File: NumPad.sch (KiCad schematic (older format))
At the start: 63 parts, among them J1 Micro_SD_Card_Det, SW1 SW_SPST, SW10 SW_SPST, SW11 SW_SPST, SW12 SW_SPST, SW13 SW_SPST, SW14 SW_SPST, SW15 SW_SPST, SW16 SW_SPST, SW17 SW_SPST, SW18 SW_SPST, SW19 SW_SPST, SW2 SW_SPST, SW20 SW_SPST, SW21 SW_SPST, SW22 SW_SPST, SW23 SW_SPST, SW24 SW_SPST, SW3 SW_SPST, SW4 SW_SPST, SW5 SW_SPST, SW6 SW_SPST, SW7 SW_SPST, SW8 SW_SPST, SW9 SW_SPST, U1 LM117_TO3, U2 STM32F072C8Tx

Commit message: Update
Update before removing matrice
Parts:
- removed U?: UG-2864HSWEG01, symbol modules:UG-2864HSWEG01
- added J2: OLED1, symbol Connector:Conn_01x04_Female
- added J3: OLED2, symbol Connector:Conn_01x04_Female
- added J4: Conn_01x05_Female, symbol Connector:Conn_01x05_Female
- added R3, R4, R5, R6: 10K, symbol Device:R_Small
- added SW25: SW_BUTTONRESET, symbol Switch:SW_Push
- added SW26: SW_BUTTON2, symbol Switch:SW_Push
- added SW27: SW_BUTTON1, symbol Switch:SW_Push
- added SW28: SW_BOOT0, symbol Switch:SW_Push
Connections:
- net +3V3: now also J4.5 (Pin_5), R3.1, R4.1, R5.1, SW28.2
- net +5V: now also J2.4 (Pin_4), J3.4 (Pin_4)
- net GND: now also J2.3 (Pin_3), J3.3 (Pin_3), J4.4 (Pin_4), R6.2, SW25.1, SW26.2, SW27.2
- net col0: now also U2.40 (PB4)
- net col1: now also U2.41 (PB5)
- net col2: now also U2.42 (PB6)
- net col3: now also U2.43 (PB7)
- net row0: now also U2.26 (PB13)
- net row1: now also U2.27 (PB14)
- net row2: now also U2.28 (PB15)
- net row3: now also U2.29 (PA8)
- net row4: now also U2.38 (PA15)
- net row5: now also U2.39 (PB3)
- net at U2.11 (PA1): now also R4.2, SW27.1
- net at U2.13 (PA3): now also R5.2, SW26.1
- net UART1_TX: now reaches U2.30 (PA9)
- net UART1_TX: now also J4.3 (Pin_3)
- net LED_DATA_EN: now reaches U2.31 (PA10)
- net USB_DM: now reaches U2.32 (PA11)
- net USB_DP: now reaches U2.33 (PA12)
- net SYS_SWDIO: now reaches U2.34 (PA13)
- net SYS_SWDIO: now also J4.2 (Pin_2)
- net SYS_SWCLK: now reaches U2.37 (PA14)
- net SYS_SWCLK: now also J4.1 (Pin_1)
- net BOOT0: now reaches U2.44 (BOOT0)
- net SCK: now reaches U2.45 (PB8)
- net SCK: now also J2.2 (Pin_2), J3.2 (Pin_2)
- net SDA: now reaches U2.46 (PB9)
- net SDA: now also J2.1 (Pin_1), J3.1 (Pin_1)
- net at U2.7 (NRST): now also R3.2, SW25.2
- new net: R6.1, SW28.1

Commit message: Update
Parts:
- added C10, C11, C12, C13, C14, C7, C8, C9: 100nF, symbol Device:C_Small
- added D26, D27, D28, D29, D30, D31, D32, D33, D34, D35, D36, D37, D38, D39, D40, D41, D42, D43, D44, D45, D46, D47, D48, D49: SK6812MINIE, LED_SMD:LED_SK6812MINI_PLCC4_3.5x3.5mm_P1.75mm, symbol random-keyboard-parts:SK6812MINIE
- added R7, R8, R9: 10K, symbol Device:R_Small
- added RV1: 10K, symbol Device:R_POT
- added SW29: Rotary_Encoder, symbol Device:Rotary_Encoder
- added U3: 74AHCT1G08, symbol 74xGxx:74AHCT1G08
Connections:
- net D+ is gone; now on net USB_DP: D1.2 (I/O1), USB1.6 (DP1), USB1.8 (DP2)
- net GND is gone; now on net +5V: C3.2, C4.2, C5.2, C6.2, D1.1 (GND), J1.11 (SHIELD), J1.6 (VSS), J2.3 (Pin_3), J3.3 (Pin_3), J4.4 (Pin_4), R1.1, R2.1, R6.2, SW25.1, SW26.2, SW27.2, U2.1 (VBAT), U2.23 (VSS), U2.35 (VSS), U2.47 (VSS), U2.8 (VSSA), USB1.1 (GND), USB1.12 (GND), USB1.13 (SHIELD)
- net USB_DM is gone; now on net USB_DN: U2.32 (PA11)
- net +3V3: now also C10.1, C11.1, C12.1, C13.1, C14.1, C7.1, C8.1, C9.1, R8.2, R9.1, RV1.3
- net +5V: now also C1.2, C2.2, U1.1 (ADJ), C10.2, C11.2, C12.2, C13.2, C14.2, C7.2, C8.2, C9.2, D26.1 (VDD), D26.3 (VSS), D27.1 (VDD), D27.3 (VSS), D28.1 (VDD), D28.3 (VSS), D29.1 (VDD), D29.3 (VSS), D30.1 (VDD), D30.3 (VSS), D31.1 (VDD), D31.3 (VSS), D32.1 (VDD), D32.3 (VSS), D33.1 (VDD), D33.3 (VSS), D34.1 (VDD), D34.3 (VSS), D35.1 (VDD), D35.3 (VSS), D36.1 (VDD), D36.3 (VSS), D37.1 (VDD), D37.3 (VSS), D38.1 (VDD), D38.3 (VSS), D39.1 (VDD), D39.3 (VSS), D40.1 (VDD), D40.3 (VSS), D41.1 (VDD), D41.3 (VSS), D42.1 (VDD), D42.3 (VSS), D43.1 (VDD), D43.3 (VSS), D44.1 (VDD), D44.3 (VSS), D45.1 (VDD), D45.3 (VSS), D46.1 (VDD), D46.3 (VSS), D47.1 (VDD), D47.3 (VSS), D48.1 (VDD), D48.3 (VSS), D49.1 (VDD), D49.3 (VSS), R7.1, RV1.1, SW29.C, U3.3 (GND)
- net BOOT0: now also R6.1, SW28.1
- net LED_DATA_EN: now also R7.2, U3.1
- net SCK: now also U2.42 (PB6); no longer U2.45 (PB8)
- net SDA: now also U2.43 (PB7); no longer U2.46 (PB9)
- net SPI_MOSI: now also U3.2
- net VCC: now also U3.5 (VCC)
- net col0: now also U2.21 (PB10); no longer U2.40 (PB4)
- net col2: now also U2.22 (PB11); no longer U2.42 (PB6)
- net col3: now also U2.25 (PB12); no longer U2.43 (PB7)
- net row4: now also U2.12 (PA2); no longer U2.38 (PA15)
- net row5: now also U2.2 (PC13); no longer U2.39 (PB3)
- net D- renamed USB_DN
- new net: D26.2 (DOUT), D32.4 (DIN)
- new net: D26.4 (DIN), U3.4
- new net: D32.2 (DOUT), D38.4 (DIN)
- new net: D38.2 (DOUT), D44.4 (DIN)
- new net: D27.4 (DIN), D44.2 (DOUT)
- new net: D27.2 (DOUT), D33.4 (DIN)
- new net: D33.2 (DOUT), D39.4 (DIN)
- new net: D39.2 (DOUT), D45.4 (DIN)
- new net: D28.4 (DIN), D45.2 (DOUT)
- new net: D28.2 (DOUT), D34.4 (DIN)
- new net: D34.2 (DOUT), D40.4 (DIN)
- new net: D40.2 (DOUT), D46.4 (DIN)
- new net: D29.4 (DIN), D46.2 (DOUT)
- new net: D29.2 (DOUT), D35.4 (DIN)
- new net: D35.2 (DOUT), D41.4 (DIN)
- new net: D41.2 (DOUT), D47.4 (DIN)
- new net: D30.4 (DIN), D47.2 (DOUT)
- new net: D30.2 (DOUT), D36.4 (DIN)
- new net: D36.2 (DOUT), D42.4 (DIN)
- new net: D42.2 (DOUT), D48.4 (DIN)
- new net: D31.4 (DIN), D48.2 (DOUT)
- new net: D31.2 (DOUT), D37.4 (DIN)
- new net: D37.2 (DOUT), D43.4 (DIN)
- new net: D43.2 (DOUT), D49.4 (DIN)
- new net POT_SLIDER: RV1.2, U2.40 (PB4)
- new net TIM2_CH1: R8.1, SW29.A, U2.38 (PA15)
- new net TIM2_CH2: R9.2, SW29.B, U2.39 (PB3)
- no-connect marks 5 -> 16
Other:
- moved on the sheet: D10, D11, D12, D13, D14, D15, D16, D17, D18, D19, D2, D20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

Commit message: Update
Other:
- moved on the sheet: R4, R5, R6, SW26, SW27, SW28
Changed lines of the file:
@@
 L Switch:SW_Push SW27
 U 1 1 5E93AC97
-P 3300 5325
-F 0 "SW27" H 3300 5610 50  0000 C CNN
-F 1 "SW_BUTTON1" H 3300 5519 50  0000 C CNN
-F 2 "" H 3300 5525 50  0001 C CNN
-F 3 "~" H 3300 5525 50  0001 C CNN
-	1    3300 5325
+P 3575 5325
+F 0 "SW27" H 3575 5610 50  0000 C CNN
+F 1 "SW_BUTTON1" H 3575 5519 50  0000 C CNN
+F 2 "" H 3575 5525 50  0001 C CNN
+F 3 "~" H 3575 5525 50  0001 C CNN
+	1    3575 5325
 	1    0    0    -1
 $EndComp
@@
 L power:GND #PWR031
 U 1 1 5E940B20
-P 3575 5325
-F 0 "#PWR031" H 3575 5075 50  0001 C CNN
-F 1 "GND" H 3580 5152 50  0000 C CNN
-F 2 "" H 3575 5325 50  0001 C CNN
-F 3 "" H 3575 5325 50  0001 C CNN
-	1    3575 5325
-	1    0    0    -1
-$EndComp
-Wire Wire Line
-	3575 5325 3500 5325
+P 3850 5325
+F 0 "#PWR031" H 3850 5075 50  0001 C CNN
+F 1 "GND" H 3855 5152 50  0000 C CNN
+F 2 "" H 3850 5325 50  0001 C CNN
+F 3 "" H 3850 5325 50  0001 C CNN
+	1    3850 5325
+	1    0    0    -1
+$EndComp
+Wire Wire Line
+	3850 5325 3775 5325
 $Comp
 L power:+3.3V #PWR026
 U 1 1 5E945D9C
-P 2975 4850
-F 0 "#PWR026" H 2975 4700 50  0001 C CNN
-F 1 "+3.3V" H 2990 5023 50  0000 C CNN
-F 2 "" H 2975 4850 50  0001 C CNN
-F 3 "" H 2975 4850 50  0001 C CNN
-	1    2975 4850
+P 3250 4825
+F 0 "#PWR026" H 3250 4675 50  0001 C CNN
+F 1 "+3.3V" H 3265 4998 50  0000 C CNN
+F 2 "" H 3250 4825 50  0001 C CNN
+F 3 "" H 3250 4825 50  0001 C CNN
+	1    3250 4825
 	1    0    0    -1
 $EndComp
@@
 L Device:R_Small R4
 U 1 1 5E946CD8
-P 2975 5000
-F 0 "R4" H 3034 5046 50  0000 L CNN
-F 1 "10K" H 3034 4955 50  0000 L CNN
-F 2 "" H 2975 5000 50  0001 C CNN
-F 3 "~" H 2975 5000 50  0001 C CNN
-	1    2975 5000
-	1    0    0    -1
-$EndComp
-Wire Wire Line
-	2975 4850 2975 4900
+P 3250 4975
+F 0 "R4" H 3309 5021 50  0000 L CNN
+F 1 "10K" H 3309 4930 50  0000 L CNN
+F 2 "" H 3250 4975 50  0001 C CNN
+F 3 "~" H 3250 4975 50  0001 C CNN
+	1    3250 4975
+	1    0    0    -1
+$EndComp
+Wire Wire Line
+	3250 4825 3250 4875
 $Comp
 L Switch:SW_Push SW26
 U 1 1 5E9524FE
-P 3275 5925
-F 0 "SW26" H 3275 6210 50  0000 C CNN
-F 1 "SW_BUTTON2" H 3275 6119 50  0000 C CNN
-F 2 "" H 3275 6125 50  0001 C CNN
-F 3 "~" H 3275 6125 50  0001 C CNN
-	1    3275 5925
+P 3550 6125
+F 0 "SW26" H 3550 6410 50  0000 C CNN
+F 1 "SW_BUTTON2" H 3550 6319 50  0000 C CNN
+F 2 "" H 3550 6325 50  0001 C CNN
+F 3 "~" H 3550 6325 50  0001 C CNN
+	1    3550 6125
 	1    0    0    -1
 $EndComp
@@
 L power:GND #PWR032
 U 1 1 5E953574
-P 3575 5925
-F 0 "#PWR032" H 3575 5675 50  0001 C CNN
-F 1 "GND" H 3580 5752 50  0000 C CNN
-F 2 "" H 3575 5925 50  0001 C CNN
-F 3 "" H 3575 5925 50  0001 C CNN
-	1    3575 5925
-	1    0    0    -1
-$EndComp
-Wire Wire Line
-	3575 5925 3475 5925
+P 3850 6125
+F 0 "#PWR032" H 3850 5875 50  0001 C CNN
+F 1 "GND" H 3855 5952 50  0000 C CNN
+F 2 "" H 3850 6125 50  0001 C CNN
+F 3 "" H 3850 6125 50  0001 C CNN
+	1    3850 6125
+	1    0    0    -1
+$EndComp
+Wire Wire Line
+	3850 6125 3750 6125
 $Comp
 L power:+3.3V #PWR027
 U 1 1 5E95E2CA
-P 2975 5600
-F 0 "#PWR027" H 2975 5450 50  0001 C CNN
-F 1 "+3.3V" H 2990 5773 50  0000 C CNN
-F 2 "" H 2975 5600 50  0001 C CNN
-F 3 "" H 2975 5600 50  0001 C CNN
-	1    2975 5600
+P 3250 5825
+F 0 "#PWR027" H 3250 5675 50  0001 C CNN
+F 1 "+3.3V" H 3265 5998 50  0000 C CNN
+F 2 "" H 3250 5825 50  0001 C CNN
+F 3 "" H 3250 5825 50  0001 C CNN
+	1    3250 5825
 	1    0    0    -1
 $EndComp
@@
 L Device:R_Small R5
 U 1 1 5E95E6BD
-P 2975 5700
-F 0 "R5" H 2825 5800 50  0000 L CNN
-F 1 "10K" H 2775 5700 50  0000 L CNN
-F 2 "" H 2975 5700 50  0001 C CNN
-F 3 "~" H 2975 5700 50  0001 C CNN
-	1    2975 5700
-	1    0    0    -1
-$EndComp
-Wire Wire Line
-	3075 5925 2975 5925
-Wire Wire Line
-	2975 5925 2975 5800
+P 3250 5925
+F 0 "R5" H 3100 6025 50  0000 L CNN
+F 1 "10K" H 3050 5925 50  0000 L CNN
+F 2 "" H 3250 5925 50  0001 C CNN
+F 3 "~" H 3250 5925 50  0001 C CNN
+	1    3250 5925
+	1    0    0    -1
+$EndComp
 Wire Wire Line
 	2475 5800 2975 5800
-Connection ~ 2975 5800
-Wire Wire Line
-	3100 5325 2975 5325
-Wire Wire Line
-	2975 5100 2975 5325
-Connection ~ 2975 5325
-Wire Wire Line
-	2975 5325 2775 5325
 $Comp
 L power:GND #PWR024
@@
 L Switch:SW_Push SW28
 U 1 1 5E9A10FB
-P 3550 6625
-F 0 "SW28" H 3550 6910 50  0000 C CNN
-F 1 "SW_BOOT0" H 3550 6819 50  0000 C CNN
-F 2 "" H 3550 6825 50  0001 C CNN
-F 3 "~" H 3550 6825 50  0001 C CNN
-	1    3550 6625
+P 3700 7175
+F 0 "SW28" H 3700 7460 50  0000 C CNN
+F 1 "SW_BOOT0" H 3700 7369 50  0000 C CNN
+F 2 "" H 3700 7375 50  0001 C CNN
+F 3 "~" H 3700 7375 50  0001 C CNN
+	1    3700 7175
 	1    0    0    -1
 $EndComp
@@
 L power:+3.3V #PWR033
 U 1 1 5E9A1D5F
-P 3875 6625
-F 0 "#PWR033" H 3875 6475 50  0001 C CNN
-F 1 "+3.3V" H 3890 6798 50  0000 C CNN
-F 2 "" H 3875 6625 50  0001 C CNN
-F 3 "" H 3875 6625 50  0001 C CNN
-	1    3875 6625
-	1    0    0    -1
-$EndComp
-Wire Wire Line
-	3875 6625 3750 6625
+P 4025 7175
+F 0 "#PWR033" H 4025 7025 50  0001 C CNN
+F 1 "+3.3V" H 4040 7348 50  0000 C CNN
+F 2 "" H 4025 7175 50  0001 C CNN
+F 3 "" H 4025 7175 50  0001 C CNN
+	1    4025 7175
+	1    0    0    -1
+$EndComp
+Wire Wire Line
+	4025 7175 3900 7175
 $Comp
 L Device:R_Small R6
 U 1 1 5E9A85E3
-P 3300 6725
-F 0 "R6" H 3150 6825 50  0000 L CNN
-F 1 "10K" H 3100 6725 50  0000 L CNN
-F 2 "" H 3300 6725 50  0001 C CNN
-F 3 "~" H 3300 6725 50  0001 C CNN
-	1    3300 6725
-	1    0    0    -1
-$EndComp
-Wire Wire Line
-	3300 6625 3350 6625
+P 3450 7275
+F 0 "R6" H 3300 7375 50  0000 L CNN
+F 1 "10K" H 3250 7275 50  0000 L CNN
+F 2 "" H 3450 7275 50  0001 C CNN
+F 3 "~" H 3450 7275 50  0001 C CNN
+	1    3450 7275
+	1    0    0    -1
+$EndComp
+Wire Wire Line
+	3450 7175 3500 7175
 $Comp
 L power:GND #PWR028
 U 1 1 5E9AF02C
-P 3300 6900
-F 0 "#PWR028" H 3300 6650 50  0001 C CNN
-F 1 "GND" H 3305 6727 50  0000 C CNN
-F 2 "" H 3300 6900 50  0001 C CNN
-F 3 "" H 3300 6900 50  0001 C CNN
-	1    3300 6900
-	1    0    0    -1
-$EndComp
-Wire Wire Line
-	3300 6825 3300 6900
+P 3450 7450
+F 0 "#PWR028" H 3450 7200 50  0001 C CNN
+F 1 "GND" H 3455 7277 50  0000 C CNN
+F 2 "" H 3450 7450 50  0001 C CNN
+F 3 "" H 3450 7450 50  0001 C CNN
+	1    3450 7450
+	1    0    0    -1
+$EndComp
+Wire Wire Line
+	3450 7375 3450 7450
 $Comp
 L power:GND #PWR034
@@
 Text GLabel 1175 6100 0    50   Input ~ 0
 SCK
-Text GLabel 3300 6450 1    50   Input ~ 0
+Text GLabel 3450 7000 1    50   Input ~ 0
 BOOT0
 Wire Wire Line
-	3300 6450 3300 6625
-Connection ~ 3300 6625
+	3450 7000 3450 7175
+Connection ~ 3450 7175
 $Comp
 L random-keyboard-parts:SK6812MINIE D26
@@
 NoConn ~ 1175 6300
 NoConn ~ 1175 6400
-NoConn ~ 3775 5050
+NoConn ~ 12950 150
+Wire Wire Line
+	2975 6125 3250 6125
+Wire Wire Line
+	2975 5800 2975 6125
+Wire Wire Line
+	3250 6125 3250 6025
+Connection ~ 3250 6125
+Wire Wire Line
+	3250 6125 3350 6125
+Wire Wire Line
+	3250 5325 3250 5075
+Connection ~ 3250 5325
+Wire Wire Line
+	3250 5325 3375 5325
+Wire Wire Line
+	2775 5325 3250 5325
 $EndSCHEMATC

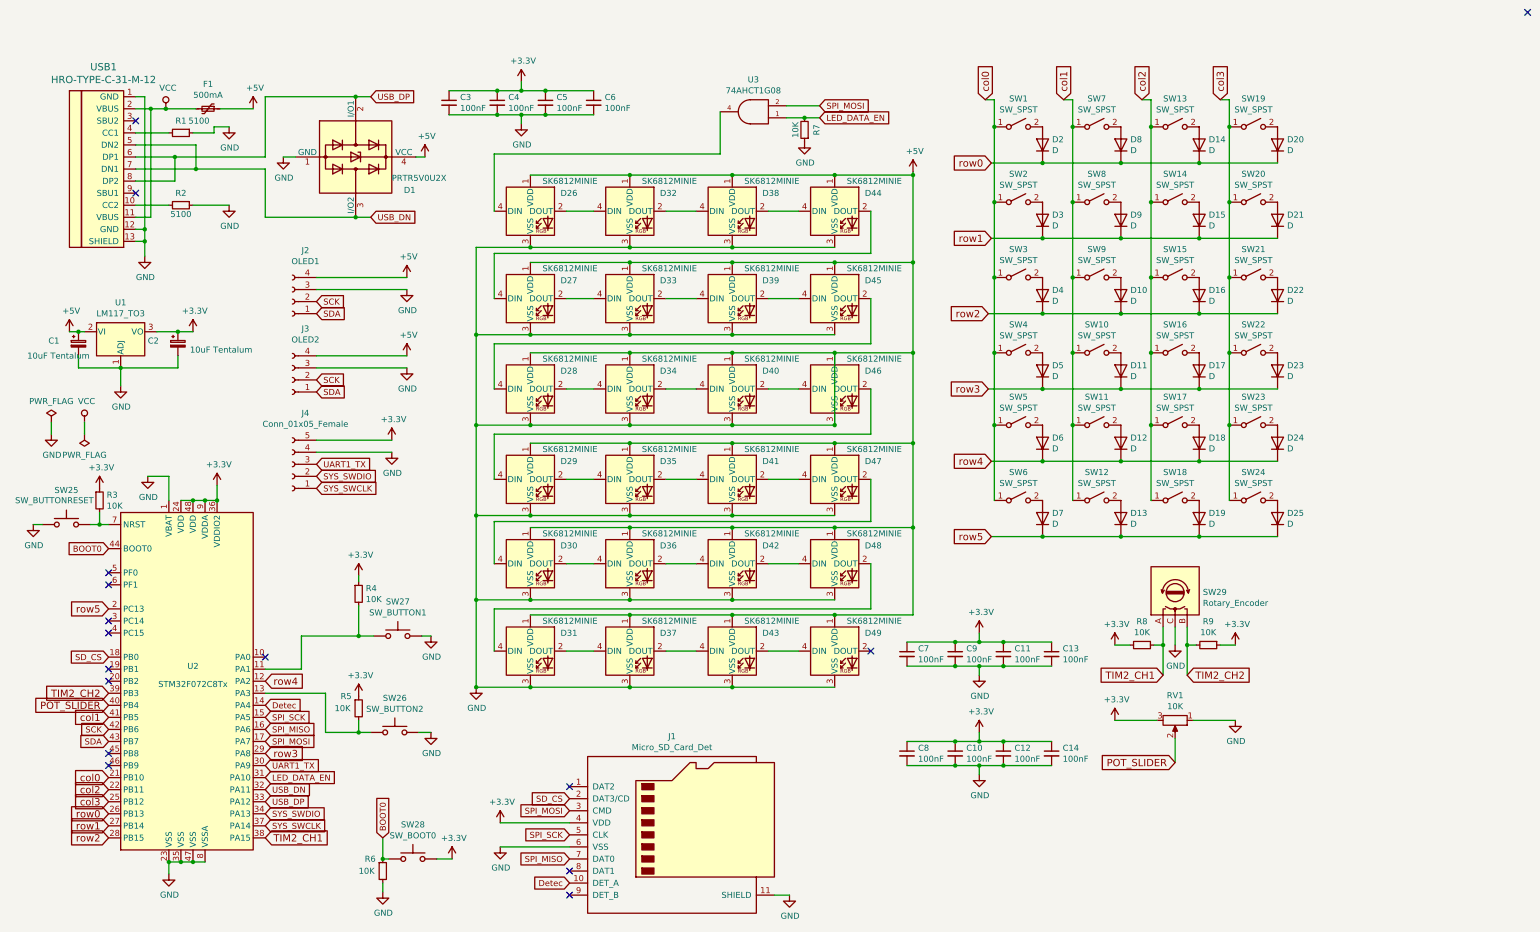
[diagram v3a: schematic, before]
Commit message: Update footprints
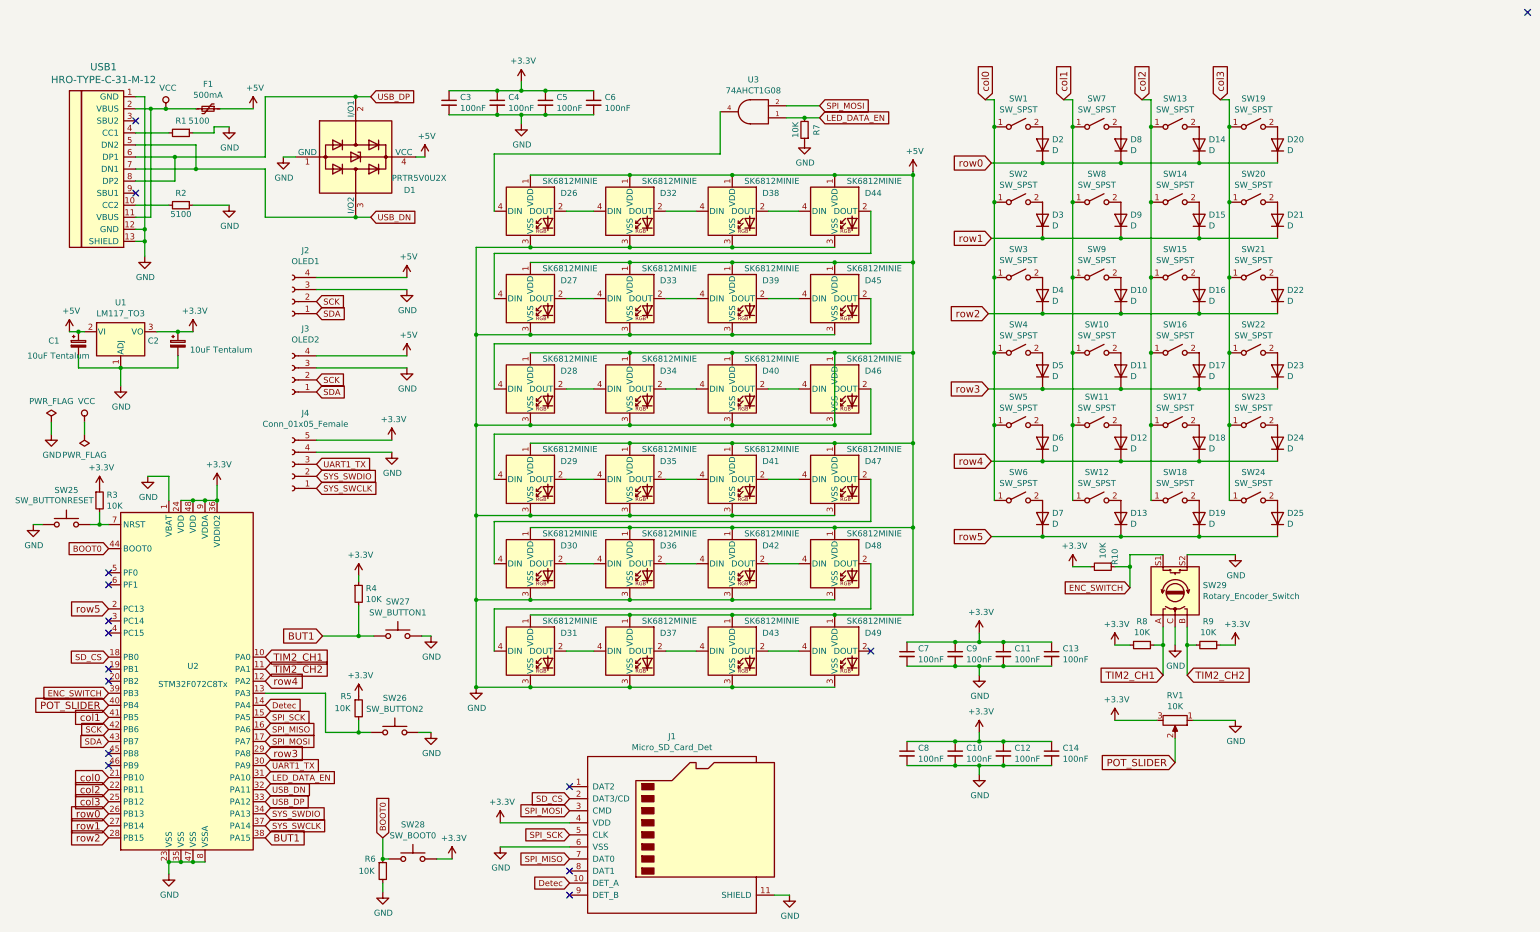
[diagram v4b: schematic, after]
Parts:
- removed SW29: Rotary_Encoder, symbol Device:Rotary_Encoder
- added R10: 10K, Resistor_SMD:R_0603_1608Metric, symbol Device:R_Small
- added SW29: Rotary_Encoder_Switch, Rotary_Encoder:RotaryEncoder_Alps_EC11E-Switch_Vertical_H20mm, symbol Device:Rotary_Encoder_Switch
- C1, C2: footprint (none) -> Capacitor_Tantalum_SMD:CP_EIA-3216-18_Kemet-A_Pad1.58x1.35mm_HandSolder
- C10, C11, C12, C13, C14, C3, C4, C5, C6, C7, C8, C9: footprint (none) -> Capacitor_SMD:C_0603_1608Metric_Pad1.05x0.95mm_HandSolder
- D10, D11, D12, D13, D14, D15, D16, D17, D18, D19, D2, D20, D21, D22, D23, D24, D25, D3, D4, D5, D6, D7, D8, D9: footprint (none) -> Diode_SMD:D_SOD-123
- F1: footprint (none) -> Fuse:Fuse_1206_3216Metric_Pad1.42x1.75mm_HandSolder
- J1: footprint (none) -> Connector_Card:microSD_HC_Molex_104031-0811
- J2, J3: footprint (none) -> Connector_PinHeader_2.54mm:PinHeader_1x04_P2.54mm_Vertical
- J4: footprint (none) -> Connector_PinHeader_2.54mm:PinHeader_1x05_P2.54mm_Vertical
- R1, R2, R3, R4, R5, R6, R7, R8, R9: footprint (none) -> Resistor_SMD:R_0603_1608Metric
- RV1: footprint (none) -> keyboard_parts:TRIM_PTA3043-2010CIA503
- SW1, SW10, SW11, SW12, SW13, SW14, SW15, SW16, SW17, SW18, SW19, SW2, SW20, SW21, SW22, SW23, SW24, SW3, SW4, SW5, SW6, SW7, SW8, SW9: footprint (none) -> MX_Only:MXOnly-1U
- SW25, SW28: footprint (none) -> random-keyboard-parts:SKQG-1155865
- SW26, SW27: footprint (none) -> keyboard_parts:TactSwitch
- U3: footprint (none) -> Package_TO_SOT_SMD:SOT-23-5_HandSoldering
- USB1: footprint (none) -> Type-C:HRO-TYPE-C-31-M-12-HandSoldering
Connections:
- net +3V3: now also R10.2
- net +5V: now also SW29.C, SW29.S2
- net TIM2_CH1: now also U2.10 (PA0), SW29.A; no longer U2.38 (PA15)
- net TIM2_CH2: now also U2.11 (PA1), SW29.B; no longer U2.39 (PB3)
- net BUT1: now reaches R4.2, SW27.1
- net BUT1: now also U2.38 (PA15); no longer U2.11 (PA1)
- new net ENC_SWITCH: R10.1, SW29.S1, U2.39 (PB3)
- no-connect marks 16 -> 15
